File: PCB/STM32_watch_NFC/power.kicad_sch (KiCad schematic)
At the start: 20 parts, among them J2 USB_C_Receptacle_PowerOnly_6P, U2 MIC5365-3.3YC5, U4 MT3608

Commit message: Kicad - Routing 4
Completed version. I just need to add graphics :)
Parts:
- added +BAT1: 2.7-4.2V, TestPoint:TestPoint_Pad_D1.5mm, symbol Connector:TestPoint
- added 5V1: 5V, TestPoint:TestPoint_Pad_D1.5mm, symbol Connector:TestPoint
- added D14: LED, LED_SMD:LED_0603_1608Metric, symbol Device:LED
- added D_BAT1: ~, TestPoint:TestPoint_Pad_D1.0mm, symbol Connector:TestPoint
- added JP1: SolderJumper_2_Open, Jumper:SolderJumper-2_P1.3mm_Open_TrianglePad1.0x1.5mm, symbol Jumper:SolderJumper_2_Open
- added R18: 510, Resistor_SMD:R_0402_1005Metric, symbol Device:R
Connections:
- net +3.3V: now also JP1.1 (A)
- net +5V: now also 5V1.1
- net +BATT: now also +BAT1.1
- net BATT: now also D_BAT1.1
- net GND: now also R18.2
- new net: D14.2 (A), JP1.2 (B)
- new net: D14.1 (K), R18.1
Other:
- note added: "Power LED"
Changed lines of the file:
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@@
   (junction (at 67.31 40.005) (diameter 0) (color 0 0 0 0)
   )
+  (junction (at 105.41 34.925) (diameter 0) (color 0 0 0 0)
+  )
   (junction (at 71.755 120.015) (diameter 0) (color 0 0 0 0)
   )
@@
   (junction (at 62.865 69.215) (diameter 0) (color 0 0 0 0)
   )
+  (junction (at 177.8 30.48) (diameter 0) (color 0 0 0 0)
+  )
   (junction (at 71.755 95.25) (diameter 0) (color 0 0 0 0)
   )
@@
     (stroke (width 0) (type default))
   )
+  (wire (pts (xy 186.055 81.915) (xy 180.975 81.915))
+    (stroke (width 0) (type default))
+  )
   (wire (pts (xy 83.82 95.25) (xy 86.36 95.25))
     (stroke (width 0) (type default))
@@
     (stroke (width 0) (type default))
   )
-  (wire (pts (xy 105.41 34.29) (xy 105.41 37.465))
+  (wire (pts (xy 105.41 34.29) (xy 105.41 34.925))
+    (stroke (width 0) (type default))
+  )
+  (wire (pts (xy 105.41 34.925) (xy 105.41 37.465))
     (stroke (width 0) (type default))
   )
@@
   )
   (wire (pts (xy 180.34 34.29) (xy 180.34 33.02))
+    (stroke (width 0) (type default))
+  )
+  (wire (pts (xy 201.93 81.915) (xy 193.675 81.915))
     (stroke (width 0) (type default))
   )
@@
     (fill (type none))
   )
+  (rectangle (start 163.195 69.215) (end 213.995 90.17)
+    (stroke (width 0) (type dash))
+    (fill (type none))
+  )
   (rectangle (start 108.585 67.31) (end 162.56 95.25)
     (stroke (width 0) (type dash))
@@
     (effects (font (size 2 2) (thickness 0.4) bold) (justify left bottom))
   )
+  (text "Power LED" (at 180.975 73.025 0)
+    (effects (font (size 2 2) (thickness 0.4) bold) (justify left bottom))
+  )
   (hierarchical_label "BATT" (shape input) (at 187.96 43.18 270) (fields_autoplaced)
     (effects (font (size 1.27 1.27)) (justify right))
@@
         (path "/e445874f-c7a3-43dd-b930-6bce1d4fa2ef/d8aa51ff-304a-4e1d-85d0-2fbe17bc154e"
           (reference "#PWR059") (unit 1)
+        )
+      )
+    )
+  )
+  (symbol (lib_id "Connector:TestPoint") (at 177.8 30.48 0) (unit 1)
+    (in_bom yes) (on_board yes) (dnp no)
+    (property "Reference" "+BAT1" (at 178.435 27.94 0)
+      (effects (font (size 1.27 1.27)) (justify left))
+    )
+    (property "Value" "2.7-4.2V" (at 168.275 26.035 0)
+      (effects (font (size 1.27 1.27)) (justify left))
+    )
+    (property "Footprint" "TestPoint:TestPoint_Pad_D1.5mm" (at 182.88 30.48 0)
+      (effects (font (size 1.27 1.27)) hide)
+    )
+    (property "Datasheet" "~" (at 182.88 30.48 0)
+      (effects (font (size 1.27 1.27)) hide)
+    )
+    (pin "1")
+    (instances
+      (project "STM32_watch_NFC"
+        (path "/e445874f-c7a3-43dd-b930-6bce1d4fa2ef/d8aa51ff-304a-4e1d-85d0-2fbe17bc154e"
+          (reference "+BAT1") (unit 1)
         )
       )
@@
     )
   )
+  (symbol (lib_id "Jumper:SolderJumper_2_Open") (at 177.165 81.915 0) (unit 1)
+    (in_bom yes) (on_board yes) (dnp no)
+    (property "Reference" "JP1" (at 176.53 79.375 0)
+      (effects (font (size 1.27 1.27)))
+    )
+    (property "Value" "SolderJumper_2_Open" (at 178.435 85.09 0)
+      (effects (font (size 1.27 1.27)))
+    )
+    (property "Footprint" "Jumper:SolderJumper-2_P1.3mm_Open_TrianglePad1.0x1.5mm" (at 177.165 81.915 0)
+      (effects (font (size 1.27 1.27)) hide)
+    )
+    (property "Datasheet" "~" (at 177.165 81.915 0)
+      (effects (font (size 1.27 1.27)) hide)
+    )
+    (pin "2")
+    (pin "1")
+    (instances
+      (project "STM32_watch_NFC"
+        (path "/e445874f-c7a3-43dd-b930-6bce1d4fa2ef/d8aa51ff-304a-4e1d-85d0-2fbe17bc154e"
+          (reference "JP1") (unit 1)
+        )
+      )
+    )
+  )
+  (symbol (lib_id "power:+3.3V") (at 173.355 81.915 90) (unit 1)
+    (in_bom yes) (on_board yes) (dnp no) (fields_autoplaced)
+    (property "Reference" "#PWR080" (at 177.165 81.915 0)
+      (effects (font (size 1.27 1.27)) hide)
+    )
+    (property "Value" "+3.3V" (at 169.545 81.915 90)
+      (effects (font (size 1.27 1.27)) (justify left))
+    )
+    (property "Footprint" "" (at 173.355 81.915 0)
+      (effects (font (size 1.27 1.27)) hide)
+    )
+    (property "Datasheet" "" (at 173.355 81.915 0)
+      (effects (font (size 1.27 1.27)) hide)
+    )
+    (pin "1")
+    (instances
+      (project "STM32_watch_NFC"
+        (path "/e445874f-c7a3-43dd-b930-6bce1d4fa2ef/d8aa51ff-304a-4e1d-85d0-2fbe17bc154e"
+          (reference "#PWR080") (unit 1)
+        )
+      )
+    )
+  )
   (symbol (lib_id "power:GND") (at 128.27 50.165 0) (unit 1)
     (in_bom yes) (on_board yes) (dnp no) (fields_autoplaced)
@@
         (path "/e445874f-c7a3-43dd-b930-6bce1d4fa2ef/d8aa51ff-304a-4e1d-85d0-2fbe17bc154e"
           (reference "#PWR016") (unit 1)
+        )
+      )
+    )
+  )
+  (symbol (lib_id "Device:R") (at 205.74 81.915 90) (unit 1)
+    (in_bom yes) (on_board yes) (dnp no)
+    (property "Reference" "R18" (at 208.28 79.375 90)
+      (effects (font (size 1.27 1.27)))
+    )
+    (property "Value" "510" (at 205.74 84.455 90)
+      (effects (font (size 1.27 1.27)))
+    )
+    (property "Footprint" "Resistor_SMD:R_0402_1005Metric" (at 205.74 83.693 90)
+      (effects (font (size 1.27 1.27)) hide)
+    )
+    (property "Datasheet" "~" (at 205.74 81.915 0)
+      (effects (font (size 1.27 1.27)) hide)
+    )
+    (property "LCSC" "C103085" (at 205.74 81.915 90)
+      (effects (font (size 1.27 1.27)) hide)
+    )
+    (pin "2")
+    (pin "1")
+    (instances
+      (project "STM32_watch_NFC"
+        (path "/e445874f-c7a3-43dd-b930-6bce1d4fa2ef/d8aa51ff-304a-4e1d-85d0-2fbe17bc154e"
+          (reference "R18") (unit 1)
         )
       )
@@
     )
   )
+  (symbol (lib_id "Device:LED") (at 189.865 81.915 180) (unit 1)
+    (in_bom yes) (on_board yes) (dnp no) (fields_autoplaced)
+    (property "Reference" "D14" (at 191.4525 74.93 0)
+      (effects (font (size 1.27 1.27)))
+    )
+    (property "Value" "LED" (at 191.4525 77.47 0)
+      (effects (font (size 1.27 1.27)))
+    )
+    (property "Footprint" "LED_SMD:LED_0603_1608Metric" (at 189.865 81.915 0)
+      (effects (font (size 1.27 1.27)) hide)
+    )
+    (property "Datasheet" "~" (at 189.865 81.915 0)
+      (effects (font (size 1.27 1.27)) hide)
+    )
+    (property "LCSC" "C84266" (at 189.865 81.915 0)
+      (effects (font (size 1.27 1.27)) hide)
+    )
+    (pin "2")
+    (pin "1")
+    (instances
+      (project "STM32_watch_NFC"
+        (path "/e445874f-c7a3-43dd-b930-6bce1d4fa2ef/d8aa51ff-304a-4e1d-85d0-2fbe17bc154e"
+          (reference "D14") (unit 1)
+        )
+      )
+    )
+  )
   (symbol (lib_id "Device:R") (at 182.245 41.275 90) (unit 1)
     (in_bom yes) (on_board yes) (dnp no)
@@
     )
   )
+  (symbol (lib_id "Connector:TestPoint") (at 105.41 34.925 270) (unit 1)
+    (in_bom yes) (on_board yes) (dnp no) (fields_autoplaced)
+    (property "Reference" "5V1" (at 110.49 33.655 90)
+      (effects (font (size 1.27 1.27)) (justify left))
+    )
+    (property "Value" "5V" (at 110.49 36.195 90)
+      (effects (font (size 1.27 1.27)) (justify left))
+    )
+    (property "Footprint" "TestPoint:TestPoint_Pad_D1.5mm" (at 105.41 40.005 0)
+      (effects (font (size 1.27 1.27)) hide)
+    )
+    (property "Datasheet" "~" (at 105.41 40.005 0)
+      (effects (font (size 1.27 1.27)) hide)
+    )
+    (pin "1")
+    (instances
+      (project "STM32_watch_NFC"
+        (path "/e445874f-c7a3-43dd-b930-6bce1d4fa2ef/d8aa51ff-304a-4e1d-85d0-2fbe17bc154e"
+          (reference "5V1") (unit 1)
+        )
+      )
+    )
+  )
   (symbol (lib_id "Device:R") (at 71.755 103.505 0) (unit 1)
     (in_bom yes) (on_board yes) (dnp no) (fields_autoplaced)
@@
         (path "/e445874f-c7a3-43dd-b930-6bce1d4fa2ef/d8aa51ff-304a-4e1d-85d0-2fbe17bc154e"
           (reference "R8") (unit 1)
+        )
+      )
+    )
+  )
+  (symbol (lib_id "Connector:TestPoint") (at 187.96 41.275 0) (unit 1)
+    (in_bom yes) (on_board yes) (dnp no)
+    (property "Reference" "D_BAT1" (at 185.42 36.195 0)
+      (effects (font (size 1.27 1.27)) (justify left))
+    )
+    (property "Value" "~" (at 178.435 36.83 0)
+      (effects (font (size 1.27 1.27)) (justify left))
+    )
+    (property "Footprint" "TestPoint:TestPoint_Pad_D1.0mm" (at 193.04 41.275 0)
+      (effects (font (size 1.27 1.27)) hide)
+    )
+    (property "Datasheet" "~" (at 193.04 41.275 0)
+      (effects (font (size 1.27 1.27)) hide)
+    )
+    (pin "1")
+    (instances
+      (project "STM32_watch_NFC"
+        (path "/e445874f-c7a3-43dd-b930-6bce1d4fa2ef/d8aa51ff-304a-4e1d-85d0-2fbe17bc154e"
+          (reference "D_BAT1") (unit 1)
         )
       )
@@
         )
       )
+    )
+  )
+  (symbol (lib_id "power:GND") (at 209.55 81.915 90) (unit 1)
+    (in_bom yes) (on_board yes) (dnp no) (fields_autoplaced)
+    (property "Reference" "#PWR092" (at 215.9 81.915 0)
+      (effects (font (size 1.27 1.27)) hide)
+    )
+    (property "Value" "GND" (at 214.63 81.915 0)
+      (effects (font (size 1.27 1.27)) hide)
+    )
+    (property "Footprint" "" (at 209.55 81.915 0)
+      (effects (font (size 1.27 1.27)) hide)
+    )
+    (property "Datasheet" "" (at 209.55 81.915 0)
+      (effects (font (size 1.27 1.27)) hide)
+    )
+    (pin "1")
+    (instances
+      (project "STM32_watch_NFC"
+        (path "/e445874f-c7a3-43dd-b930-6bce1d4fa2ef/d8aa51ff-304a-4e1d-85d0-2fbe17bc154e"
+          (reference "#PWR092") (unit 1)
+        )
+      )

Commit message: Coding LEDs
Library for led management, buttons
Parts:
- Li-po1: LCSC (none) -> C566239
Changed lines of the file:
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@@
+      (effects (font (size 1.27 1.27)) hide)
+    )
+    (property "LCSC" "C566239" (at 185.42 30.48 0)
       (effects (font (size 1.27 1.27)) hide)
     )

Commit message: CODING #5 working Time and ADC for battery value
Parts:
- R4, R5: LCSC C284599 -> C25905

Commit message: LAST NFC
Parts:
- J2: LCSC C2927283 -> C2927027
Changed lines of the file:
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@@
 			)
 		)
-		(property "LCSC" "C2927283"
+		(property "LCSC" " C2927027"
 			(at 50.165 47.625 0)
 			(effects

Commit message: URX watch #1
pcb is NOT panelizated
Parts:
- J2: LCSC C2927027 -> C2927283
- R4, R5: LCSC C25905 -> C284599
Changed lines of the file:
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@@
 			)
 		)
-		(property "LCSC" " C2927027"
+		(property "LCSC" "C2927283"
 			(at 50.165 47.625 0)
 			(effects
@@
 			)
 		)
-		(property "LCSC" "C25905"
+		(property "LCSC" "C284599"
 			(at 69.215 55.245 90)
 			(effects
@@
 			)
 		)
-		(property "LCSC" "C25905"
+		(property "LCSC" "C284599"
 			(at 69.215 52.705 90)
 			(effects

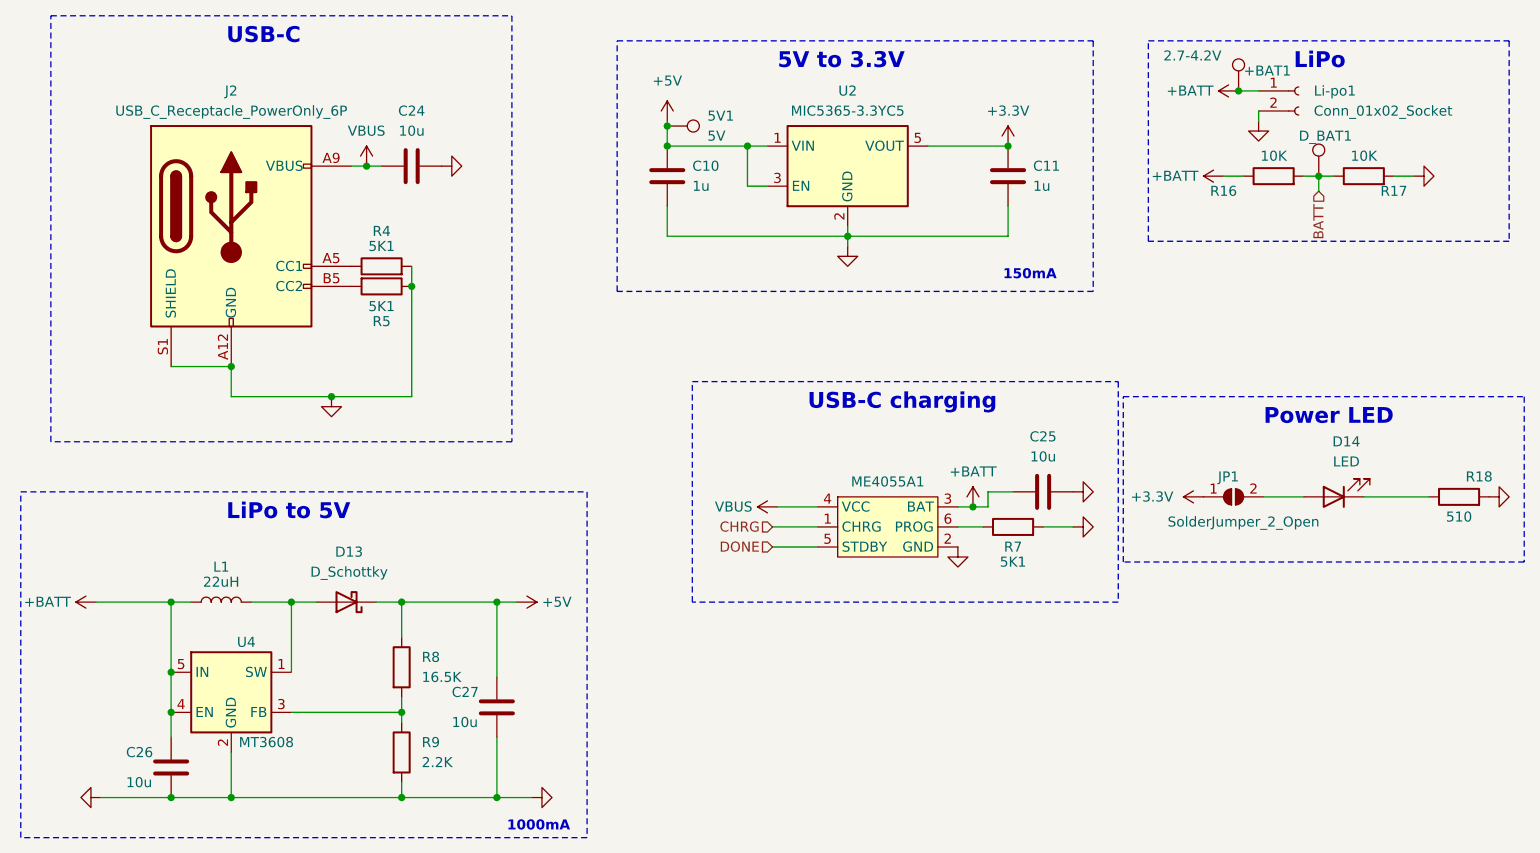
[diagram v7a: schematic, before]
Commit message: Kicad - new Routing 3
TM1637 7-segment driver
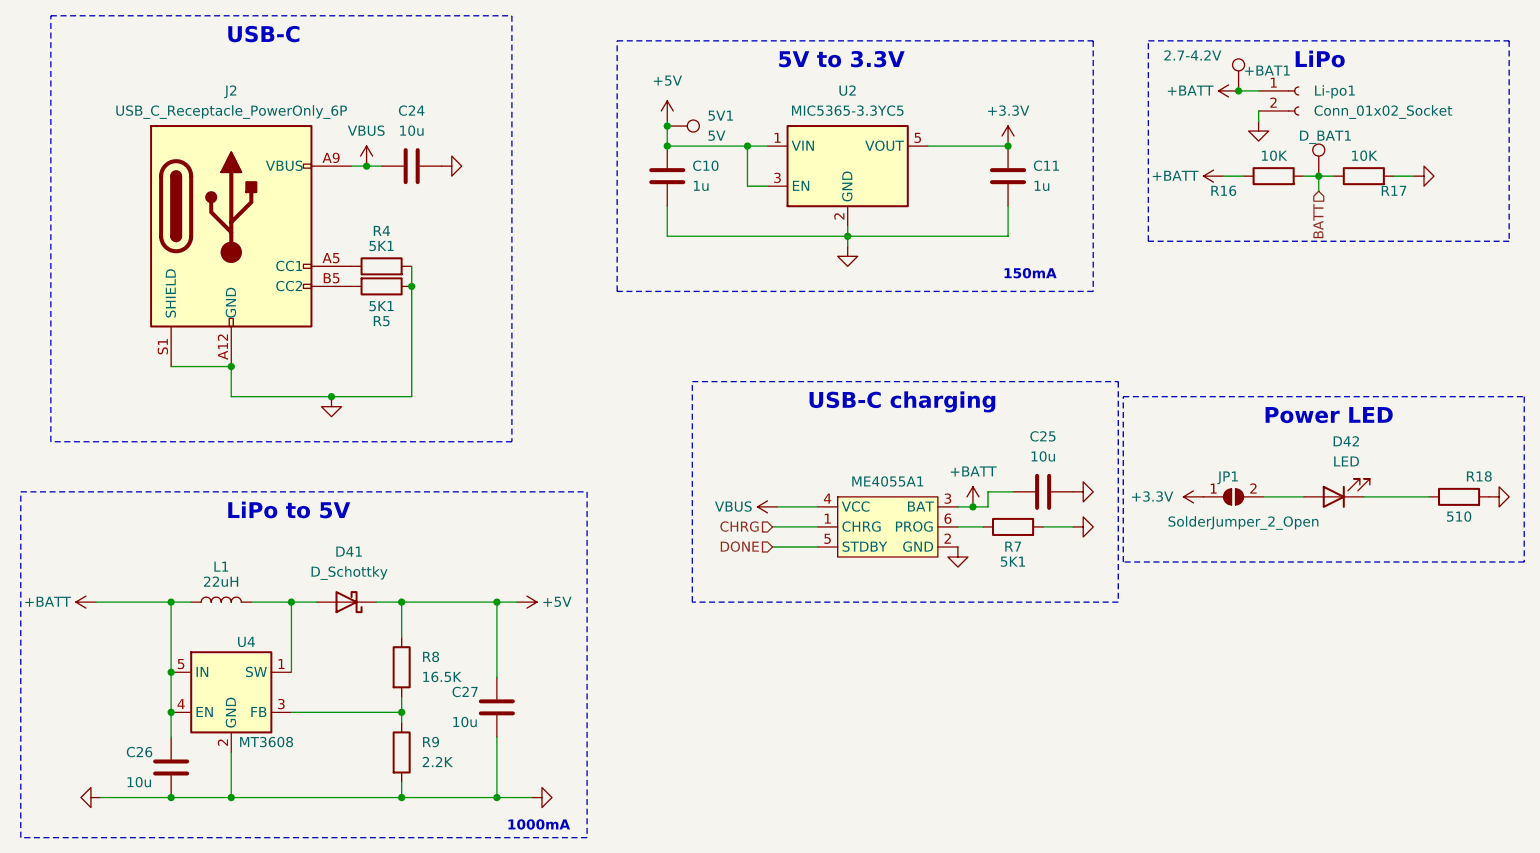
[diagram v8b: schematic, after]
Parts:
- renumbered D13 to D41, D14 to D42
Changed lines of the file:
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@@
 		(shape input)
 		(at 187.96 43.18 270)
-		(fields_autoplaced yes)
 		(effects
 			(font
@@
 		(shape input)
 		(at 118.745 85.725 180)
-		(fields_autoplaced yes)
 		(effects
 			(font
@@
 		(shape input)
 		(at 118.745 88.265 180)
-		(fields_autoplaced yes)
 		(effects
 			(font
@@
 		(dnp no)
 		(fields_autoplaced yes)
-		(property "Reference" "D13"
+		(property "Reference" "D41"
 			(at 65.0875 88.9 0)
 			(effects
@@
 			(project "STM32_watch_NFC"
 				(path "/e445874f-c7a3-43dd-b930-6bce1d4fa2ef/d8aa51ff-304a-4e1d-85d0-2fbe17bc154e"
-					(reference "D13")
+					(reference "D41")
 					(unit 1)
 				)
@@
 		(dnp no)
 		(fields_autoplaced yes)
-		(property "Reference" "D14"
+		(property "Reference" "D42"
 			(at 191.4525 74.93 0)
 			(effects
@@
 			(project "STM32_watch_NFC"
 				(path "/e445874f-c7a3-43dd-b930-6bce1d4fa2ef/d8aa51ff-304a-4e1d-85d0-2fbe17bc154e"
-					(reference "D14")
-					(unit 1)
-				)
+					(reference "D42")
+					(unit 1)
+				)
